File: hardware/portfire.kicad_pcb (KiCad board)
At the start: 2 copper layers, 100 x 100 mm, 200 parts, among them IC101 STM32F407VGT6TR, IC102 TPS62152, IC103 25AA02E48, IC104 ADP3335, IC105 SNx5176B, IC201 MAX5969x, IC202 KSZ8081RNA, IC203 MAX17503, IC301 TPS92512, J201 RJ45, J202 AUX POWER, P101 SWD_TC, P102 AUX_BUS_RX, P103 AUX_BUS_RX, P301 1, P302 2, P303 3, P304 4, P305 5, P306 6, P307 7, P308 8, P309 9, P310 10, P311 11, P312 12, P313 13, P314 14, P315 15, P316 16, P317 17, P318 18, P319 19, P320 20, P321 21, P322 22, P323 23, P324 24, P325 25, P326 26, P327 27, P328 28, P329 29, P330 30, Q301 NTR4501NT1G, Q302 NTR4501NT1G, Q303 NTR4501NT1G, Q304 NTR4501NT1G, Q305 NTR4501NT1G, Q306 NTR4501NT1G, Q307 NTR4501NT1G, Q308 NTR4501NT1G, Q309 NTR4501NT1G, Q310 NTR4501NT1G, Q311 NTR4501NT1G, Q312 NTR4501NT1G, Q313 NTR4501NT1G, Q314 NTR4501NT1G, Q315 NTR4501NT1G, Q316 NTR4501NT1G, Q317 NTR4501NT1G, Q318 NTR4501NT1G, Q319 NTR4501NT1G, Q320 NTR4501NT1G, Q321 NTR4501NT1G, Q322 NTR4501NT1G, Q323 NTR4501NT1G, Q324 NTR4501NT1G, Q325 NTR4501NT1G, Q326 NTR4501NT1G, Q327 NTR4501NT1G, Q328 NTR4501NT1G, Q329 NTR4501NT1G, Q330 NTR4501NT1G, T201 749010012A, X101 PART, X102 PART, X103 PART, X104 PART, Y101 26M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

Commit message: Lots of placement/routing
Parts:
- removed TP201: +48V, hardware:Test_point_mini
- removed TP304: BUS, hardware:Test_point_mini
- removed TP305: RETURN, hardware:Test_point_mini
- moved P103 246.6 mm to (23.8, 170.1), turned to 90 degrees
- moved C119 241.2 mm to (28.5, 168.0), turned to 0 degrees
- moved P102 239.3 mm to (23.8, 163.1), turned to 90 degrees
- moved IC105 236.6 mm to (30.7, 164.5), turned to 180 degrees
- moved C120 226.1 mm to (36.4, 170.2), turned to 0 degrees
- moved IC104 225.4 mm to (36.3, 166.2), turned to 90 degrees
- moved C118 225.1 mm to (36.2, 162.3), turned to 0 degrees
- moved C303 162.6 mm to (62.3, 160.2)
- moved R307 161.9 mm to (62.7, 162.6)
- moved C305 161.9 mm to (65.8, 162.6), turned to 0 degrees
- moved L301 161.9 mm to (69.3, 155.5)
- moved C301 161.4 mm to (53.3, 157.7)
- moved C302 161.4 mm to (58.5, 164.5)
- moved C304 161.4 mm to (56.6, 157.5)
- moved D304 161.4 mm to (58.3, 154.4)
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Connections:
- D105 pad 2: (no net) -> /LINK
- IC202 pad 23: (no net) -> /LINK
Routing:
- net /firing/RETURN: track 23.6 -> 597.9 mm, vias 0 -> 2
- net /firing/BUS: track 16.2 -> 269.7 mm, vias 0 -> 7
- net +6V: track 31.6 -> 116.8 mm
- net GND: track 121.9 -> 174.9 mm, vias 26 -> 47
- net +48V: track 9.05 -> 60.5 mm
- net Net-(C206-Pad1): track 0.00 -> 44.3 mm, vias 0 -> 3
- net Net-(C206-Pad2): track 0.00 -> 41.0 mm
- net /ethernet/DCDC_EN: track 1.86 -> 37.5 mm
- net /ethernet/VA1: track 13.7 -> 37.5 mm
- net /LINK: track 0.00 -> 23.5 mm
- net Net-(C222-Pad1): track 29.6 -> 52.9 mm
- net Net-(C304-Pad2): track 12.8 -> 34.5 mm
- net /ethernet/VA2: track 6.83 -> 25.9 mm
- net /ethernet/VB1: track 23.9 -> 42.3 mm
- net /ethernet/VB2: track 23.6 -> 41.1 mm
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- added copper zone on B.Cu, net GND
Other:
- outline, holes or cut-outs redrawn
- board text added: "+48V"
- board text added: "+5V"
- board text added: "+6V"
- board text added: "6-12 VDC"
- board text added: "LINK"

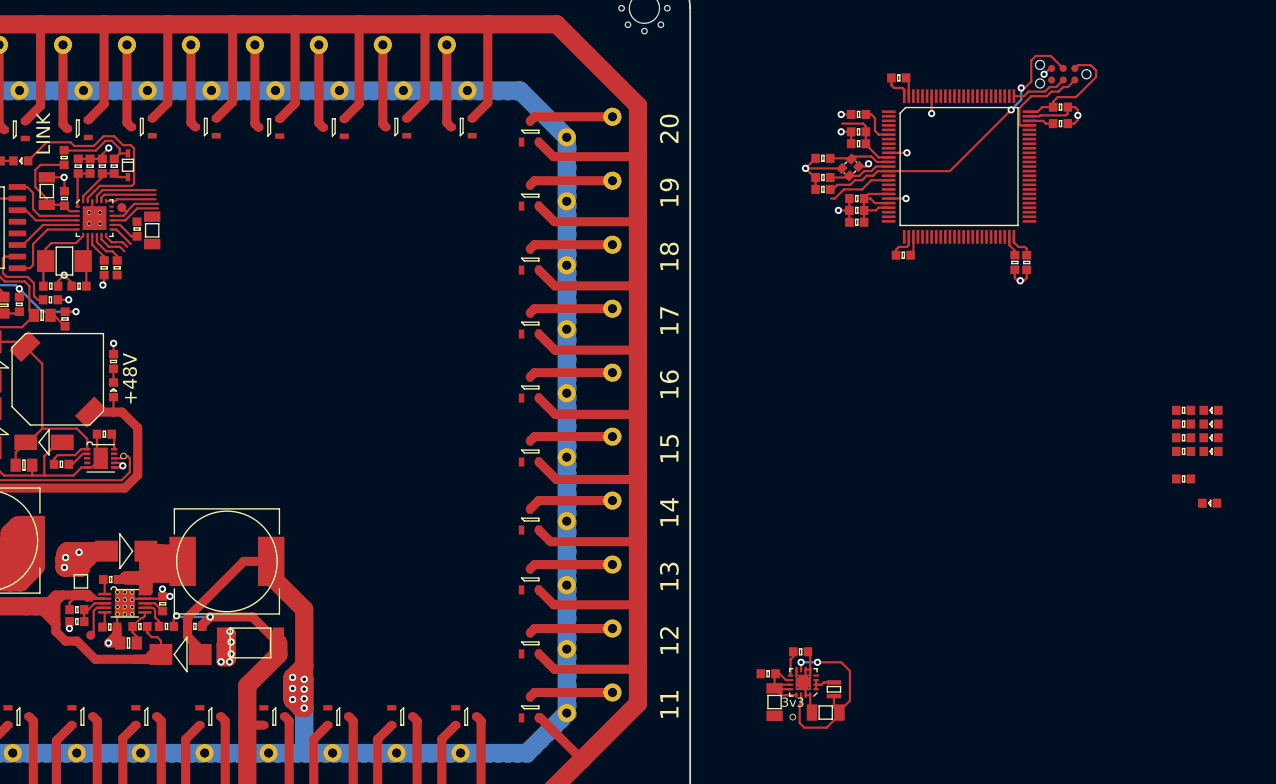
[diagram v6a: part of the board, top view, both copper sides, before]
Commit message: Placed uc, routed RMII
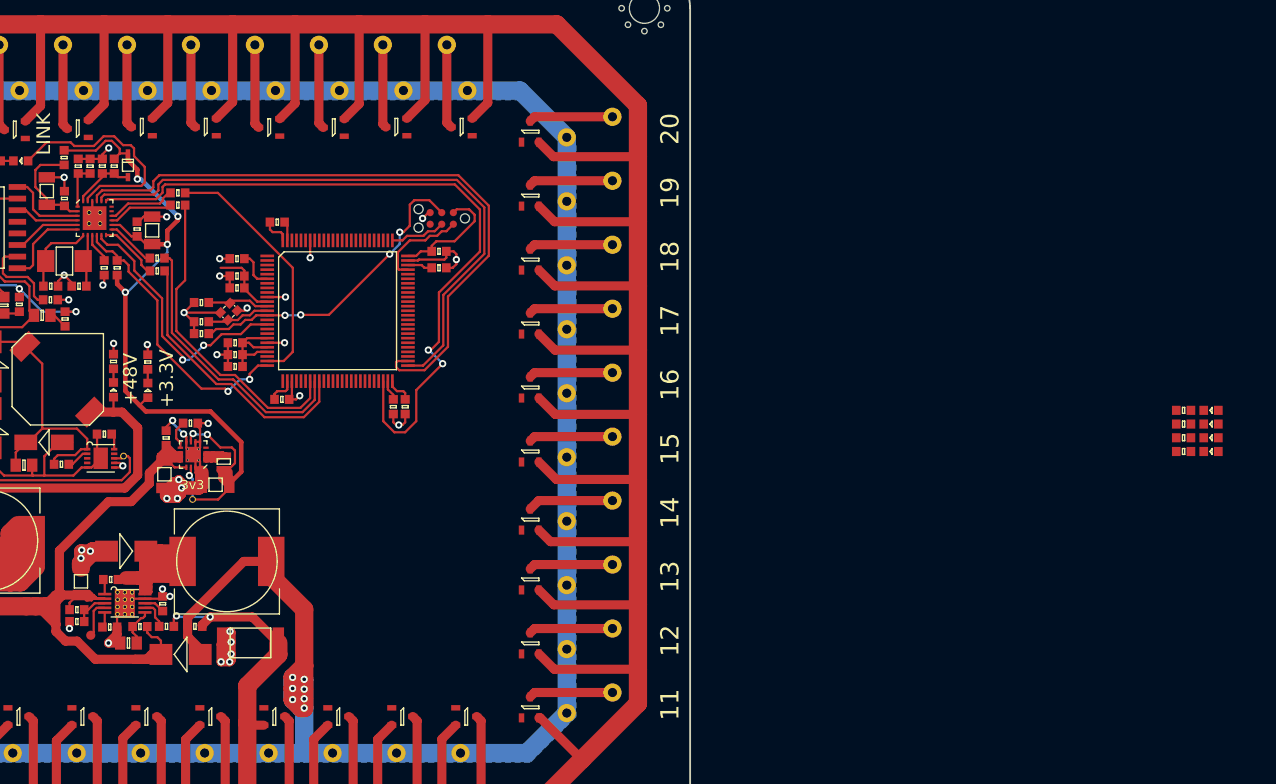
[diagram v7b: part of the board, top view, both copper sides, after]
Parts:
- removed TP204: 50MHz_CLK, agg:TESTPAD
- added R213: 33, agg:0603, F.Cu at (61.7, 123.7)
- added R214: 33, agg:0603, F.Cu at (61.7, 122.3)
- added R215: 33, agg:0603, F.Cu at (63.9, 116.5)
- added R216: 33, agg:0603, F.Cu at (63.9, 115.2)
- moved D104 116.8 mm to (60.7, 136.8), turned to 270 degrees
- moved R104 114.1 mm to (60.6, 133.7), turned to 90 degrees
- moved C116 71.3 mm to (65.3, 140.4)
- moved C117 71.3 mm to (68.1, 147.1)
- moved L101 71.3 mm to (69.0, 144.6)
- moved C114 71.3 mm to (62.5, 146.0)
- moved IC102 71.3 mm to (65.6, 143.8)
- moved C115 70.8 mm to (62.7, 142.0), turned to 90 degrees
- moved TP101 69.9 mm to (65.5, 148.8)
- moved C113 69.8 mm to (75.3, 137.8)
- moved C110 69.8 mm to (74.8, 118.4)
- moved C111 69.8 mm to (88.8, 138.6)
- moved C123 69.8 mm to (66.5, 129.3)
- moved P101 69.8 mm to (92.8, 118.0)
- moved C101 69.8 mm to (66.5, 130.6)
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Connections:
- D104 pad 2: (no net) -> 3v3
- IC202 pad 12: /RMII_RXD1 -> Net-(IC202-Pad12)
- IC202 pad 13: /RMII_RXD0 -> Net-(IC202-Pad13)
- IC202 pad 15: /RMII_CRS_DV -> Net-(IC202-Pad15)
- IC202 pad 16: /RMII_REF_CLK -> Net-(IC202-Pad16)
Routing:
- net /RMII_TX_EN: track 5.50 -> 79.7 mm, vias 0 -> 2
- net /RMII_TXD1: track 7.26 -> 72.2 mm
- net 3v3: track 80.3 -> 141.9 mm, vias 2 -> 8
- net /RMII_TXD0: track 6.43 -> 66.5 mm
- net +6V: track 116.8 -> 146.0 mm
- net /RMII_CRS_DV: track 5.65 -> 34.6 mm
- net /RMII_RXD0: track 2.77 -> 30.9 mm
- net /RMII_RXD1: track 2.94 -> 30.5 mm
- net /RMII_MDIO: track 4.31 -> 31.4 mm, vias 0 -> 2
- net GND: track 174.9 -> 197.7 mm, vias 47 -> 56
- net /RMII_REF_CLK: track 6.56 -> 27.6 mm
- net /RMII_MDC: track 10.7 -> 28.9 mm, vias 0 -> 2
- net Net-(IC102-Pad1): track 3.05 -> 11.6 mm
- net Net-(IC202-Pad16): track 0.00 -> 7.89 mm
- net Net-(IC202-Pad15): track 0.00 -> 7.14 mm
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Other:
- board text added: "+3.3V"

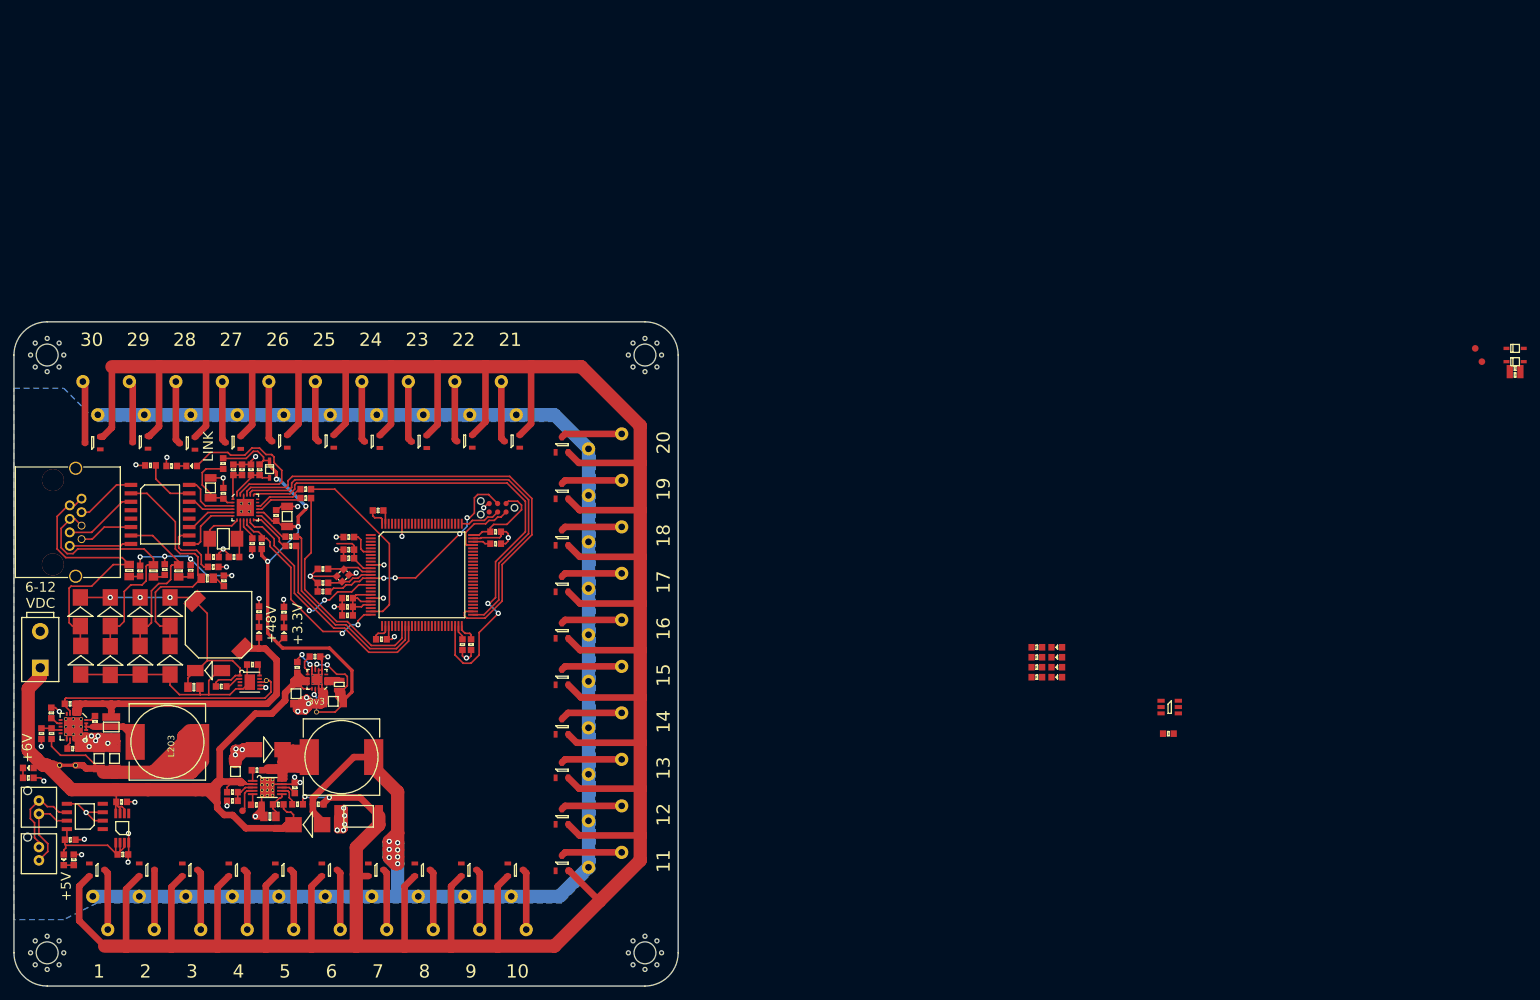
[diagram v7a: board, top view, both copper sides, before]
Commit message: Routed ROM
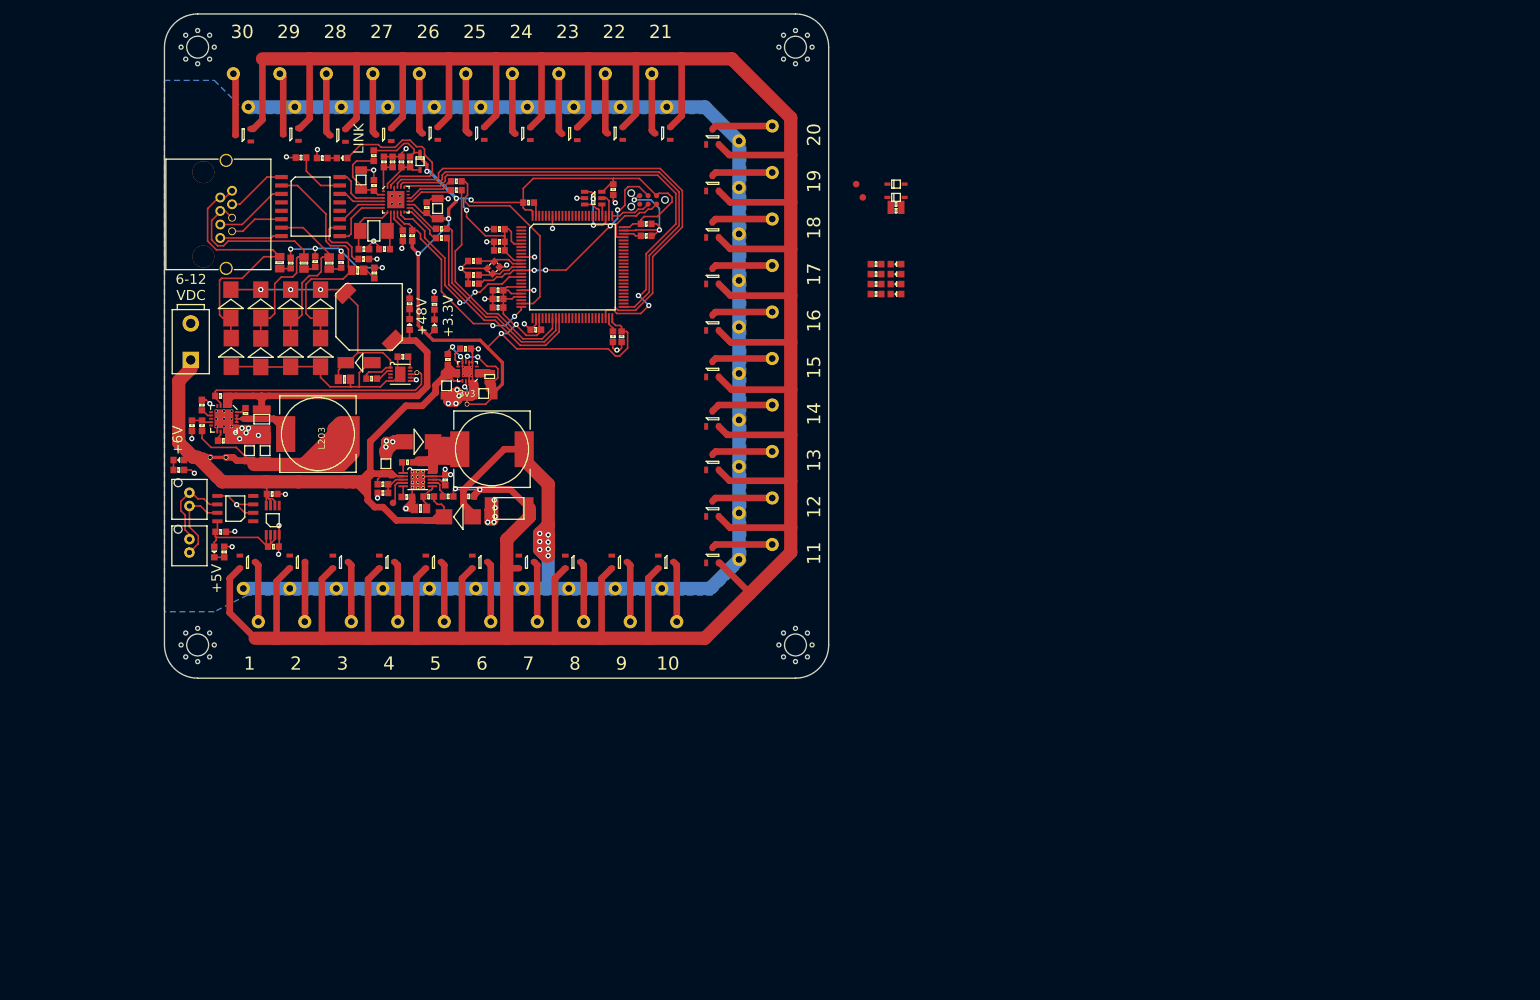
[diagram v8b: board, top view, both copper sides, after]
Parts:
- moved C121 117.0 mm to (110.2, 70.1), turned to 270 degrees
- moved IC103 115.8 mm to (107.2, 71.4)
- moved D301 96.4 mm to (152.8, 69.3)
- moved D302 96.4 mm to (152.8, 71.3)
- moved R304 96.4 mm to (152.8, 72.3)
- moved R306 96.4 mm to (152.8, 73.3)
- moved TP301 96.4 mm to (146.8, 69.3)
- moved TP303 96.4 mm to (147.8, 71.3)
- moved D106 62.6 mm to (152.8, 85.8)
- moved D107 62.6 mm to (152.8, 84.3)
- moved D108 62.6 mm to (152.8, 82.8)
- moved D109 62.6 mm to (152.8, 81.3)
- moved R106 62.6 mm to (149.8, 85.8)
- moved R107 62.6 mm to (149.8, 84.3)
- moved R108 62.6 mm to (149.8, 82.8)
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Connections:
- IC101 pad 77: (no net) -> /ROM_CS
- IC101 pad 78: (no net) -> /ROM_SCK
- IC101 pad 79: (no net) -> /ROM_MISO
- IC101 pad 80: (no net) -> /ROM_MOSI
- IC103 pad 1: (no net) -> /ROM_SCK
- IC103 pad 3: (no net) -> /ROM_MOSI
- IC103 pad 4: (no net) -> /ROM_MISO
- IC103 pad 5: (no net) -> /ROM_CS
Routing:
- net 3v3: track 141.9 -> 224.6 mm, vias 8 -> 11
- net GND: track 197.7 -> 208.2 mm, vias 56 -> 59
- net /ROM_SCK: track 0.00 -> 9.16 mm, vias 0 -> 2
- net /RMII_TX_EN: track 79.7 -> 71.6 mm
- net /ROM_CS: track 0.00 -> 3.51 mm
- net /ROM_MOSI: track 0.00 -> 3.44 mm
- net /RMII_REF_CLK: track 27.6 -> 29.6 mm
- net /RMII_TXD1: track 72.2 -> 70.4 mm
- net /ROM_MISO: track 0.00 -> 1.75 mm
